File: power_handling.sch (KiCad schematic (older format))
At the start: 50 parts, among them J1 Power In, U1 LM27762, U10 74LS32, U11 ADG734, U12 LM1085-5V, U13 ADG734, U14 ADG734, U15 LM27762, U16 ADG734, U2 ADG715, U3 LMZ34002, U4 ADG715, U5 74LS32, U6 LM1084, U7 TS12A44514, U8 TS12A44514, U9 ADG715

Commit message: Finalized footprint assignment. ready for pcb time
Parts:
- R1, R10, R11, R12, R13, R2, R3, R4, R5, R6, R7, R8, R9: footprint (none) -> Resistor_SMD:R_0603_1608Metric_Pad0.84x1.00mm_HandSolder
- U1, U15: footprint (none) -> Package_SON:WSON-12-1EP_3x2mm_P0.5mm
- U10, U5: footprint Housings_SSOP:SSOP-14_5.3x6.2mm_Pitch0.65mm -> Package_SSOP:TSSOP-14_4.4x5mm_P0.65mm
- U11, U13, U14, U16: footprint Housings_SSOP:TSSOP-20_4.4x6.5mm_Pitch0.65mm -> Package_SSOP:TSSOP-20_4.4x6.5mm_P0.65mm
- U12, U6: footprint TO_SOT_Packages_THT:TO-220_Horizontal -> Package_TO_SOT_SMD:TO-263-3_TabPin4
- U2, U4, U9: footprint Housings_SSOP:TSSOP-24_4.4x7.8mm_Pitch0.65mm -> Package_SSOP:TSSOP-24_4.4x7.8mm_P0.65mm
- U3: footprint (none) -> SW-Texas:RKG_(S-PB1QFN-N41)
- U7, U8: footprint Housings_SSOP:TSSOP-14_4.4x5mm_Pitch0.65mm -> Package_SSOP:TSSOP-14_4.4x5mm_P0.65mm
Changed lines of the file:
@@
 F 0 "U7" H 3828 2847 60  0000 C CNN
 F 1 "TS12A44514" H 3828 2741 60  0000 C CNN
-F 2 "Housings_SSOP:TSSOP-14_4.4x5mm_Pitch0.65mm" H 4000 3850 60  0001 C CNN
+F 2 "Package_SSOP:TSSOP-14_4.4x5mm_P0.65mm" H 4000 3850 60  0001 C CNN
 F 3 "" H 3650 2500 60  0001 C CNN
 F 4 "0.00@0" H 3550 3550 60  0001 C CNN "Pricing"
@@
 F 0 "U8" H 3828 2659 60  0000 C CNN
 F 1 "TS12A44514" H 3828 2553 60  0000 C CNN
-F 2 "Housings_SSOP:TSSOP-14_4.4x5mm_Pitch0.65mm" H 4000 4200 60  0001 C CNN
+F 2 "Package_SSOP:TSSOP-14_4.4x5mm_P0.65mm" H 4000 4200 60  0001 C CNN
 F 3 "" H 3650 2850 60  0001 C CNN
 F 4 "0.00@0" H 3550 3900 60  0001 C CNN "Pricing"
@@
 F 0 "U6" H 8000 2300 60  0000 C CNN
 F 1 "LM1084" H 8000 2200 60  0000 C CNN
-F 2 "TO_SOT_Packages_THT:TO-220_Horizontal" H 7900 2400 60  0001 C CNN
+F 2 "Package_TO_SOT_SMD:TO-263-3_TabPin4" H 7900 2400 60  0001 C CNN
 F 3 "http://www.ti.com/lit/ds/symlink/lm1084.pdf" H 8300 3400 60  0001 C CNN
 F 4 "5A, 3.3V, 5V, Adj Vout" H 8200 3200 60  0001 C CNN "Characteristics"
@@
 F 0 "U12" H 7750 3997 60  0000 C CNN
 F 1 "LM1085-5V" H 7750 3891 60  0000 C CNN
-F 2 "TO_SOT_Packages_THT:TO-220_Horizontal" H 7650 3550 60  0001 C CNN
+F 2 "Package_TO_SOT_SMD:TO-263-3_TabPin4" H 7650 3550 60  0001 C CNN
 F 3 "http://www.ti.com/lit/ds/symlink/lm1085.pdf" H 8050 4550 60  0001 C CNN
 F 4 "3A, 3.3V, 5V, 12V, Adj Vout" H 7950 4350 60  0001 C CNN "Characteristics"
@@
 F 0 "U10" H 5580 3296 50  0000 L CNN
 F 1 "74LS32" H 5580 3205 50  0000 L CNN
-F 2 "Housings_SSOP:SSOP-14_5.3x6.2mm_Pitch0.65mm" H 5350 3250 50  0001 C CNN
+F 2 "Package_SSOP:TSSOP-14_4.4x5mm_P0.65mm" H 5350 3250 50  0001 C CNN
 F 3 "" H 5350 3250 50  0001 C CNN
 	5    5350 3250
@@
 F 0 "U5" H 5580 2546 50  0000 L CNN
 F 1 "74LS32" H 5580 2455 50  0000 L CNN
-F 2 "Housings_SSOP:SSOP-14_5.3x6.2mm_Pitch0.65mm" H 5350 2500 50  0001 C CNN
+F 2 "Package_SSOP:TSSOP-14_4.4x5mm_P0.65mm" H 5350 2500 50  0001 C CNN
 F 3 "" H 5350 2500 50  0001 C CNN
 	5    5350 2500
@@
 F 0 "U2" H 1872 2003 60  0000 L CNN
 F 1 "ADG715" H 1872 1897 60  0000 L CNN
-F 2 "Housings_SSOP:TSSOP-24_4.4x7.8mm_Pitch0.65mm" H 1900 2900 60  0001 C CNN
+F 2 "Package_SSOP:TSSOP-24_4.4x7.8mm_P0.65mm" H 1900 2900 60  0001 C CNN
 F 3 "http://www.analog.com/media/en/technical-documentation/data-sheets/ADG714_715.pdf" H 1900 3000 60  0001 C CNN
 F 4 "0.00@0" H 1700 3550 60  0001 C CNN "Pricing"
@@
 F 0 "U4" H 1872 2503 60  0000 L CNN
 F 1 "ADG715" H 1872 2397 60  0000 L CNN
-F 2 "Housings_SSOP:TSSOP-24_4.4x7.8mm_Pitch0.65mm" H 1900 3400 60  0001 C CNN
+F 2 "Package_SSOP:TSSOP-24_4.4x7.8mm_P0.65mm" H 1900 3400 60  0001 C CNN
 F 3 "http://www.analog.com/media/en/technical-documentation/data-sheets/ADG714_715.pdf" H 1900 3500 60  0001 C CNN
 F 4 "0.00@0" H 1700 4050 60  0001 C CNN "Pricing"
@@
 F 0 "U11" H 1897 3403 60  0000 L CNN
 F 1 "ADG734" H 1897 3297 60  0000 L CNN
-F 2 "Housings_SSOP:TSSOP-20_4.4x6.5mm_Pitch0.65mm" H 1750 4350 60  0001 C CNN
+F 2 "Package_SSOP:TSSOP-20_4.4x6.5mm_P0.65mm" H 1750 4350 60  0001 C CNN
 F 3 "http://www.analog.com/media/en/technical-documentation/data-sheets/ADG733_734.pdf" H 1450 4250 60  0001 C CNN
 F 4 "0.00@0" H 1650 3850 60  0001 C CNN "Pricing"
@@
 F 0 "U13" H 1897 3903 60  0000 L CNN
 F 1 "ADG734" H 1897 3797 60  0000 L CNN
-F 2 "Housings_SSOP:TSSOP-20_4.4x6.5mm_Pitch0.65mm" H 1750 4850 60  0001 C CNN
+F 2 "Package_SSOP:TSSOP-20_4.4x6.5mm_P0.65mm" H 1750 4850 60  0001 C CNN
 F 3 "http://www.analog.com/media/en/technical-documentation/data-sheets/ADG733_734.pdf" H 1450 4750 60  0001 C CNN
 F 4 "0.00@0" H 1650 4350 60  0001 C CNN "Pricing"
@@
 F 0 "U14" H 1897 4403 60  0000 L CNN
 F 1 "ADG734" H 1897 4297 60  0000 L CNN
-F 2 "Housings_SSOP:TSSOP-20_4.4x6.5mm_Pitch0.65mm" H 1750 5350 60  0001 C CNN
+F 2 "Package_SSOP:TSSOP-20_4.4x6.5mm_P0.65mm" H 1750 5350 60  0001 C CNN
 F 3 "http://www.analog.com/media/en/technical-documentation/data-sheets/ADG733_734.pdf" H 1450 5250 60  0001 C CNN
 F 4 "0.00@0" H 1650 4850 60  0001 C CNN "Pricing"
@@
 F 0 "U16" H 1897 4903 60  0000 L CNN
 F 1 "ADG734" H 1897 4797 60  0000 L CNN
-F 2 "Housings_SSOP:TSSOP-20_4.4x6.5mm_Pitch0.65mm" H 1750 5850 60  0001 C CNN
+F 2 "Package_SSOP:TSSOP-20_4.4x6.5mm_P0.65mm" H 1750 5850 60  0001 C CNN
 F 3 "http://www.analog.com/media/en/technical-documentation/data-sheets/ADG733_734.pdf" H 1450 5750 60  0001 C CNN
 F 4 "0.00@0" H 1650 5350 60  0001 C CNN "Pricing"
@@
 F 0 "U9" H 1872 3003 60  0000 L CNN
 F 1 "ADG715" H 1872 2897 60  0000 L CNN
-F 2 "Housings_SSOP:TSSOP-24_4.4x7.8mm_Pitch0.65mm" H 1900 3900 60  0001 C CNN
+F 2 "Package_SSOP:TSSOP-24_4.4x7.8mm_P0.65mm" H 1900 3900 60  0001 C CNN
 F 3 "http://www.analog.com/media/en/technical-documentation/data-sheets/ADG714_715.pdf" H 1900 4000 60  0001 C CNN
 F 4 "0.00@0" H 1700 4550 60  0001 C CNN "Pricing"
@@
 F 0 "U1" H 13850 2547 60  0000 C CNN
 F 1 "LM27762" H 13850 2441 60  0000 C CNN
-F 2 "" H 13650 2550 60  0001 C CNN
+F 2 "Package_SON:WSON-12-1EP_3x2mm_P0.5mm" H 13650 2550 60  0001 C CNN
 F 3 "http://www.ti.com/lit/ds/symlink/lm27762.pdf" H 13850 2750 60  0001 C CNN
 F 4 "0.00@0" H 13850 3250 60  0001 C CNN "Pricing"
@@
 F 0 "R3" H 14809 1846 50  0000 L CNN
 F 1 "68kΩ 5%" H 14809 1755 50  0000 L CNN
-F 2 "" H 14750 1800 50  0001 C CNN
+F 2 "Resistor_SMD:R_0603_1608Metric_Pad0.84x1.00mm_HandSolder" H 14750 1800 50  0001 C CNN
 F 3 "" H 14750 1800 50  0001 C CNN
 	1    14750 1800
@@
 F 0 "R2" H 14859 1646 50  0000 L CNN
 F 1 "75kΩ 5%" H 14859 1555 50  0000 L CNN
-F 2 "" H 14800 1600 50  0001 C CNN
+F 2 "Resistor_SMD:R_0603_1608Metric_Pad0.84x1.00mm_HandSolder" H 14800 1600 50  0001 C CNN
 F 3 "" H 14800 1600 50  0001 C CNN
 	1    14800 1600
@@
 F 0 "R6" H 14909 2246 50  0000 L CNN
 F 1 "75kΩ 5%" H 14909 2155 50  0000 L CNN
-F 2 "" H 14850 2200 50  0001 C CNN
+F 2 "Resistor_SMD:R_0603_1608Metric_Pad0.84x1.00mm_HandSolder" H 14850 2200 50  0001 C CNN
 F 3 "" H 14850 2200 50  0001 C CNN
 	1    14850 2200
@@
 F 0 "R4" H 14859 2046 50  0000 L CNN
 F 1 "68kΩ 5%" H 14859 1955 50  0000 L CNN
-F 2 "" H 14800 2000 50  0001 C CNN
+F 2 "Resistor_SMD:R_0603_1608Metric_Pad0.84x1.00mm_HandSolder" H 14800 2000 50  0001 C CNN
 F 3 "" H 14800 2000 50  0001 C CNN
 	1    14800 2000
@@
 F 0 "R1" H 13108 1546 50  0000 L CNN
 F 1 "10kΩ" H 13108 1455 50  0000 L CNN
-F 2 "" H 13050 1500 50  0001 C CNN
+F 2 "Resistor_SMD:R_0603_1608Metric_Pad0.84x1.00mm_HandSolder" H 13050 1500 50  0001 C CNN
 F 3 "" H 13050 1500 50  0001 C CNN
 	1    13050 1500
@@
 F 0 "U15" H 13750 5147 60  0000 C CNN
 F 1 "LM27762" H 13750 5041 60  0000 C CNN
-F 2 "" H 13550 5150 60  0001 C CNN
+F 2 "Package_SON:WSON-12-1EP_3x2mm_P0.5mm" H 13550 5150 60  0001 C CNN
 F 3 "http://www.ti.com/lit/ds/symlink/lm27762.pdf" H 13750 5350 60  0001 C CNN
 F 4 "0.00@0" H 13750 5850 60  0001 C CNN "Pricing"
@@
 F 0 "R11" H 14659 4446 50  0000 L CNN
 F 1 "68kΩ 5%" H 14659 4355 50  0000 L CNN
-F 2 "" H 14600 4400 50  0001 C CNN
+F 2 "Resistor_SMD:R_0603_1608Metric_Pad0.84x1.00mm_HandSolder" H 14600 4400 50  0001 C CNN
 F 3 "" H 14600 4400 50  0001 C CNN
 	1    14600 4400
@@
 F 0 "R10" H 14708 4246 50  0000 L CNN
 F 1 "220kΩ 5%" H 14708 4155 50  0000 L CNN
-F 2 "" H 14650 4200 50  0001 C CNN
+F 2 "Resistor_SMD:R_0603_1608Metric_Pad0.84x1.00mm_HandSolder" H 14650 4200 50  0001 C CNN
 F 3 "" H 14650 4200 50  0001 C CNN
 	1    14650 4200
@@
 F 0 "R13" H 14758 4846 50  0000 L CNN
 F 1 "220kΩ 5%" H 14758 4755 50  0000 L CNN
-F 2 "" H 14700 4800 50  0001 C CNN
+F 2 "Resistor_SMD:R_0603_1608Metric_Pad0.84x1.00mm_HandSolder" H 14700 4800 50  0001 C CNN
 F 3 "" H 14700 4800 50  0001 C CNN
 	1    14700 4800
@@
 F 0 "R12" H 14709 4646 50  0000 L CNN
 F 1 "68kΩ 5%" H 14709 4555 50  0000 L CNN
-F 2 "" H 14650 4600 50  0001 C CNN
+F 2 "Resistor_SMD:R_0603_1608Metric_Pad0.84x1.00mm_HandSolder" H 14650 4600 50  0001 C CNN
 F 3 "" H 14650 4600 50  0001 C CNN
 	1    14650 4600
@@
 F 0 "R9" H 13008 4146 50  0000 L CNN
 F 1 "10kΩ" H 13008 4055 50  0000 L CNN
-F 2 "" H 12950 4100 50  0001 C CNN
+F 2 "Resistor_SMD:R_0603_1608Metric_Pad0.84x1.00mm_HandSolder" H 12950 4100 50  0001 C CNN
 F 3 "" H 12950 4100 50  0001 C CNN
 	1    12950 4100
@@
 F 0 "U3" H 10650 3100 60  0000 R CNN
 F 1 "LMZ34002" H 11500 2450 60  0000 R CNN
-F 2 "" H 11200 2950 60  0001 C CNN
+F 2 "SW-Texas:RKG_(S-PB1QFN-N41)" H 11200 2950 60  0001 C CNN
 F 3 "http://www.ti.com/lit/ds/symlink/lmz34002.pdf" H 11400 3400 60  0001 C CNN
 F 4 "0.00@0" H 11300 3700 60  0001 C CNN "Pricing"
@@
 F 0 "R5" H 10159 2196 50  0000 L CNN
 F 1 "174kΩ 1% 63mW" H 10159 2105 50  0000 L CNN
-F 2 "" H 10100 2150 50  0001 C CNN
+F 2 "Resistor_SMD:R_0603_1608Metric_Pad0.84x1.00mm_HandSolder" H 10100 2150 50  0001 C CNN
 F 3 "" H 10100 2150 50  0001 C CNN
 F 4 "Vishay-Dale" H 10100 2150 60  0001 C CNN "Manufacturer"
@@
 F 0 "R7" H 10109 2396 50  0000 L CNN
 F 1 "22.6kΩ 1% 63mW" H 10109 2305 50  0000 L CNN
-F 2 "" H 10050 2350 50  0001 C CNN
+F 2 "Resistor_SMD:R_0603_1608Metric_Pad0.84x1.00mm_HandSolder" H 10050 2350 50  0001 C CNN
 F 3 "" H 10050 2350 50  0001 C CNN
 F 4 "Vishay-Dale" H 10050 2350 60  0001 C CNN "Manufacturer"
@@
 F 0 "R8" H 10409 3096 50  0000 L CNN
 F 1 "143kΩ 1% 63mW" H 10409 3005 50  0000 L CNN
-F 2 "" H 10350 3050 50  0001 C CNN
+F 2 "Resistor_SMD:R_0603_1608Metric_Pad0.84x1.00mm_HandSolder" H 10350 3050 50  0001 C CNN
 F 3 "" H 10350 3050 50  0001 C CNN
 F 4 "Vishay-Dale" H 10350 3050 60  0001 C CNN "Manufacturer"

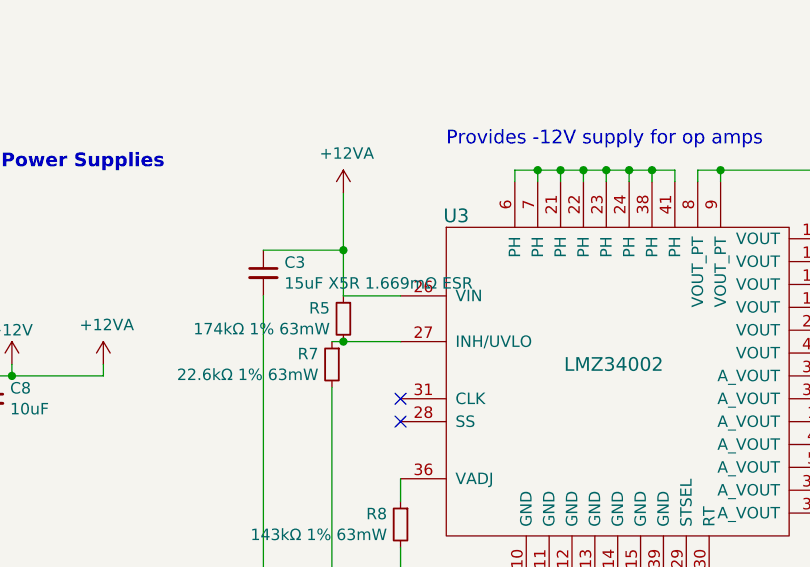
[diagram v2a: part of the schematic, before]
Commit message: Fix non printing characters in descriptions
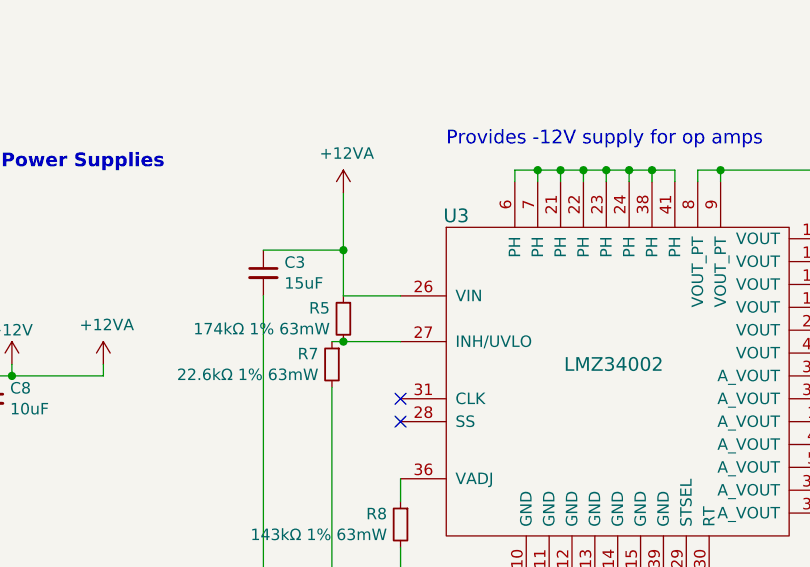
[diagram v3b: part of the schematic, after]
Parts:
- C3: value 15uF X5R 1.669mΩ ESR -> 15uF; Manufacturer Part Number (none) -> C2012X5R1V156M125AC; Notes C2012X5R1V156M125AC -> X5R 1.669mΩ ESR
- U11, U13, U14, U16: Description CMOS, 2.5 Low Voltage, Quad SPDT Switch -> CMOS, 2.5 Low Voltage, Quad SPDT Switch
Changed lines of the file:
@@
 F 4 "0.00@0" H 1650 3850 60  0001 C CNN "Pricing"
 F 5 "Analog Devices" H 1700 4150 60  0001 C CNN "Manufacturer"
-F 6 "CMOS, 2.5 Low Voltage, Quad SPDT Switch" H 1600 3950 60  0001 C CNN "Description"
+F 6 "CMOS, 2.5 Low Voltage, Quad SPDT Switch" H 1600 3950 60  0001 C CNN "Description"
 F 7 "TSSOP20" H 1650 4050 60  0001 C CNN "Package ID"
 	5    1650 3400
@@
 F 4 "0.00@0" H 1650 4350 60  0001 C CNN "Pricing"
 F 5 "Analog Devices" H 1700 4650 60  0001 C CNN "Manufacturer"
-F 6 "CMOS, 2.5 Low Voltage, Quad SPDT Switch" H 1600 4450 60  0001 C CNN "Description"
+F 6 "CMOS, 2.5 Low Voltage, Quad SPDT Switch" H 1600 4450 60  0001 C CNN "Description"
 F 7 "TSSOP20" H 1650 4550 60  0001 C CNN "Package ID"
 	5    1650 3900
@@
 F 4 "0.00@0" H 1650 4850 60  0001 C CNN "Pricing"
 F 5 "Analog Devices" H 1700 5150 60  0001 C CNN "Manufacturer"
-F 6 "CMOS, 2.5 Low Voltage, Quad SPDT Switch" H 1600 4950 60  0001 C CNN "Description"
+F 6 "CMOS, 2.5 Low Voltage, Quad SPDT Switch" H 1600 4950 60  0001 C CNN "Description"
 F 7 "TSSOP20" H 1650 5050 60  0001 C CNN "Package ID"
 	5    1650 4400
@@
 F 4 "0.00@0" H 1650 5350 60  0001 C CNN "Pricing"
 F 5 "Analog Devices" H 1700 5650 60  0001 C CNN "Manufacturer"
-F 6 "CMOS, 2.5 Low Voltage, Quad SPDT Switch" H 1600 5450 60  0001 C CNN "Description"
+F 6 "CMOS, 2.5 Low Voltage, Quad SPDT Switch" H 1600 5450 60  0001 C CNN "Description"
 F 7 "TSSOP20" H 1650 5550 60  0001 C CNN "Package ID"
 	5    1650 4900
@@
 P 9750 1950
 F 0 "C3" H 9842 1996 50  0000 L CNN
-F 1 "15uF X5R 1.669mΩ ESR" H 9842 1905 50  0000 L CNN
+F 1 "15uF" H 9842 1905 50  0000 L CNN
 F 2 "Capacitor_SMD:C_0805_2012Metric_Pad1.15x1.50mm_HandSolder" H 9750 1950 50  0001 C CNN
 F 3 "" H 9750 1950 50  0001 C CNN
@@
 F 5 "Ceramic Capacitor" H 9750 1950 60  0001 C CNN "Description"
 F 6 "0805" H 9750 1950 60  0001 C CNN "Package ID"
-F 7 "C2012X5R1V156M125AC" H 9750 1950 60  0001 C CNN "Notes"
+F 7 "X5R 1.669mΩ ESR" H 9750 1950 60  0001 C CNN "Notes"
 F 8 "0.00@0" H 9750 1950 60  0001 C CNN "Pricing"
+F 9 "C2012X5R1V156M125AC" H 9750 1950 60  0001 C CNN "Manufacturer Part Number"
 	1    9750 1950
 	1    0    0    -1
